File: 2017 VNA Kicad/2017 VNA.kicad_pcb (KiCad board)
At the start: 2 copper layers, 50 x 30 mm, 48 parts, among them P1 Output, P2 Input, U1 SI5351A, U2 NL7WB66, Y1 CX3225

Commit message: Our board changes
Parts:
- removed G***: LOGO, SMA:LOGO
- removed Osc1: Jumper, Resistors_SMD:R_0805
- removed R12, R13, R14, R15: 5.1k, Resistors_SMD:R_0805
- removed R16: 160, Resistors_SMD:R_0805
- removed R17: 16k, Resistors_SMD:R_0805
- removed Ref1, Test1: Jumper, Pin_Headers:Pin_Header_Straight_2x01_Pitch2.54mm
- added JP_Osc1: Osc, Pin_Headers:Pin_Header_Straight_1x02_Pitch2.54mm, F.Cu at (95.4, 93.5)
- added JP_Ref1: Ref, Pin_Headers:Pin_Header_Straight_1x02_Pitch2.54mm, F.Cu at (78.7, 88.9)
- added JP_Test1: Test, Pin_Headers:Pin_Header_Straight_1x02_Pitch2.54mm, F.Cu at (98.4, 89.6)
- added L2: 1mH, Inductors_SMD:L_1210, F.Cu at (109.5, 80.2)
- added L3: 1mH, Inductors_SMD:L_1210, F.Cu at (87.1, 76.7)
- added R3: 56, Resistors_SMD:R_0805, F.Cu at (89.3, 94.8)
- added R5: INF, Resistors_SMD:R_0805, F.Cu at (84.2, 76.0)
- added R6: 50k, Resistors_SMD:R_0805, F.Cu at (101.4, 73.4)
- C10: value 1nF -> .68uF; moved to F.Cu
- C11: value 10uF -> 0pF; moved to F.Cu
- C12: value 0.1uF -> .68uF
- C13, C6, C7, C9, L1: moved to F.Cu
- C15: value 1nF -> 27pF; moved to F.Cu
- C16: value 1nF -> 27pF
- C3: moved to B.Cu
- C8: value 1nF -> 1uF
- R10: value 16k -> 330; moved to F.Cu
- R11: value 10k -> 220; moved to F.Cu
- R4: value 51 -> INF; moved to F.Cu
- R7: value 5.1k -> 50k
- R8: value 5.1k -> 1000k; moved to F.Cu
- R9: value 5.1k -> 1000k
- moved C10 29.5 mm to (106.7, 78.1), turned to 90 degrees
- moved C3 26.0 mm to (77.4, 74.7)
- moved C6 24.0 mm to (106.7, 82.3)
- moved R8 22.3 mm to (97.4, 72.2), turned to 270 degrees
- moved R4 21.5 mm to (103.8, 72.2), turned to 90 degrees
- moved R10 20.5 mm to (91.1, 72.3), turned to 90 degrees
- moved C13 20.3 mm to (99.4, 72.2), turned to 90 degrees
- moved C15 18.0 mm to (95.0, 72.3), turned to 270 degrees
- moved C11 17.7 mm to (93.1, 72.3), turned to 270 degrees
- moved A_GND1 16.3 mm to (91.6, 75.2)
- moved R11 13.0 mm to (91.3, 79.8), turned to 270 degrees
- moved C7 12.0 mm to (98.3, 93.4), turned to 270 degrees
- moved R1 11.4 mm to (88.4, 85.4), turned to 0 degrees
- moved L1 10.1 mm to (87.3, 81.9), turned to 270 degrees
- moved R2 10.1 mm to (84.6, 84.9), turned to 270 degrees
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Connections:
- R4 pad 1: Net-(C6-Pad1) -> Net-(C10-Pad1)
- R4 pad 2: Net-(R4-Pad2) -> GND
- R7 pad 1: Net-(C8-Pad1) -> Net-(C14-Pad1)
- R7 pad 2: Net-(R7-Pad2) -> Net-(C12-Pad1)
- R8 pad 1: Net-(C10-Pad1) -> /A13
- R8 pad 2: Net-(C6-Pad1) -> Net-(C13-Pad1)
- R9 pad 1: Net-(C12-Pad1) -> /A14
- R9 pad 2: Net-(C8-Pad1) -> Net-(C14-Pad1)
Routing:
- net GND: track 246.1 -> 284.2 mm, vias 122 -> 95
- net /A13: track 9.62 -> 36.1 mm
- net Net-(C8-Pad1): track 5.72 -> 24.8 mm, vias 0 -> 1
- net Net-(C9-Pad1): track 7.33 -> 23.6 mm
- net Net-(C4-Pad2): track 5.33 -> 20.3 mm, vias 0 -> 2
- net /Ref_In: track 2.00 -> 13.4 mm, vias 0 -> 1
- net Net-(A_GND1-Pad1): track 8.57 -> 19.2 mm
- net Net-(C6-Pad1): track 5.95 -> 16.5 mm, vias 0 -> 1
- net Net-(C1-Pad2): track 17.6 -> 26.1 mm, vias 0 -> 1
- net Net-(C10-Pad1): track 5.78 -> 13.2 mm
- net /Test_In: track 14.3 -> 21.6 mm
- net /A14: track 9.69 -> 16.7 mm
- net /SDA: track 39.2 -> 44.4 mm
- net Net-(C7-Pad1): track 7.68 -> 12.1 mm
- net Net-(R7-Pad2): track 2.92 -> 0.00 mm
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
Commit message: Trying this again
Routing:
- net GND: track 284.2 -> 298.1 mm, vias 95 -> 94
- net +3V3: track 74.5 -> 76.5 mm

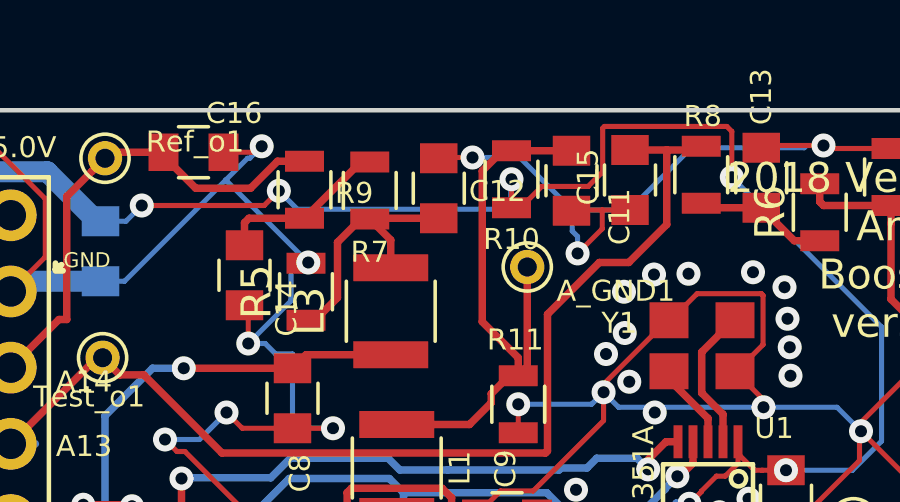
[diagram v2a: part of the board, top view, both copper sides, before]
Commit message: Fix all DRC errors
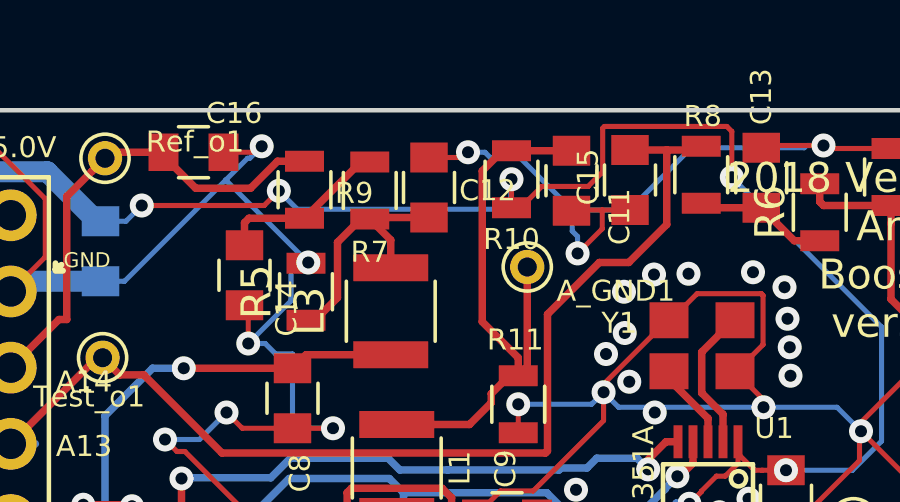
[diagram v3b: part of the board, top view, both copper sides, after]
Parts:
- moved C12 0.33 mm to (88.3, 72.6)
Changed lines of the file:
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@@
     (thickness 1.6)
     (drawings 28)
-    (tracks 654)
+    (tracks 658)
     (zones 0)
     (modules 46)
@@
   )
   (module Capacitors_SMD:C_0805 (layer F.Cu)
-    (at 88.675 72.6 90)
+    (at 88.35 72.575 90)
     (descr "Capacitor SMD 0805, reflow soldering, AVX (see smccp.pdf)")
     (tags "capacitor 0805")
@@
   (segment (start 93.302638 74.206364) (end 93.125 74.028726) (width 0.17) (layer B.Cu) (net 1))
   (segment (start 93.302638 74.772049) (end 93.302638 74.206364) (width 0.17) (layer B.Cu) (net 1))
-  (segment (start 89.8 71.575) (end 91.375 71.575) (width 0.17) (layer B.Cu) (net 1))
-  (via (at 89.8 71.575) (size 0.8) (drill 0.4) (layers F.Cu B.Cu) (net 1))
   (segment (start 88.7 71.575) (end 88.675 71.6) (width 0.17) (layer F.Cu) (net 1))
-  (segment (start 89.8 71.575) (end 88.7 71.575) (width 0.17) (layer F.Cu) (net 1))
   (via (at 82.773497 71.201198) (size 0.8) (drill 0.4) (layers F.Cu B.Cu) (net 1))
   (segment (start 81.5 71.4) (end 82.574695 71.4) (width 0.17) (layer F.Cu) (net 1))
@@
   (segment (start 82.890685 77.775) (end 83.240685 78.125) (width 0.17) (layer B.Cu) (net 1))
   (segment (start 82.325 77.775) (end 82.890685 77.775) (width 0.17) (layer B.Cu) (net 1))
+  (via (at 89.65 71.4) (size 0.8) (drill 0.4) (layers F.Cu B.Cu) (net 1))
+  (segment (start 88.35 71.575) (end 89.475 71.575) (width 0.17) (layer F.Cu) (net 1))
+  (segment (start 89.475 71.575) (end 89.65 71.4) (width 0.17) (layer F.Cu) (net 1))
+  (segment (start 90.390685 71.575) (end 91.375 71.575) (width 0.17) (layer B.Cu) (net 1))
+  (segment (start 90.215685 71.4) (end 90.390685 71.575) (width 0.17) (layer B.Cu) (net 1))
+  (segment (start 89.65 71.4) (end 90.215685 71.4) (width 0.17) (layer B.Cu) (net 1))
   (segment (start 73.319999 72.050001) (end 71.87 73.5) (width 0.7) (layer B.Cu) (net 2))
   (segment (start 75.625001 72.050001) (end 73.319999 72.050001) (width 0.7) (layer B.Cu) (net 2))
@@
   (segment (start 103.75 73.175) (end 101.5 73.175) (width 0.25) (layer F.Cu) (net 54))
   (segment (start 86.4 73.6) (end 86.375 73.625) (width 0.25) (layer F.Cu) (net 55))
-  (segment (start 88.675 73.6) (end 86.4 73.6) (width 0.25) (layer F.Cu) (net 55))
   (segment (start 84.55 77) (end 85.3 76.25) (width 0.25) (layer F.Cu) (net 55))
   (segment (start 84.25 77) (end 84.55 77) (width 0.25) (layer F.Cu) (net 55))
@@
   (segment (start 91.625 78.55) (end 91.325 78.85) (width 0.25) (layer F.Cu) (net 18))
   (segment (start 91.625 75.225) (end 91.625 78.55) (width 0.25) (layer F.Cu) (net 18))
+  (segment (start 86.425 73.575) (end 86.375 73.625) (width 0.25) (layer F.Cu) (net 55))
+  (segment (start 88.35 73.575) (end 86.425 73.575) (width 0.25) (layer F.Cu) (net 55))
   (zone (net 1) (net_name GND) (layer B.Cu) (hatch edge 0.508)
     (connect_pads (clearance 0.508))
     (min_thickness 0.254)
-    (fill (arc_segments 16) (thermal_gap 0.508) (thermal_bridge_width 0.508))
+    (fill yes (arc_segments 16) (thermal_gap 0.508) (thermal_bridge_width 0.508))
     (polygon
       (pts
@@
     (connect_pads (clearance 0.508))
     (min_thickness 0.254)
-    (fill (arc_segments 16) (thermal_gap 0.508) (thermal_bridge_width 0.508))
+    (fill yes (arc_segments 16) (thermal_gap 0.508) (thermal_bridge_width 0.508))
     (polygon
       (pts
@@
     (connect_pads (clearance 0.508))
     (min_thickness 0.254)
-    (fill (arc_segments 16) (thermal_gap 0.508) (thermal_bridge_width 0.508))
+    (fill yes (arc_segments 16) (thermal_gap 0.508) (thermal_bridge_width 0.508))
     (polygon
       (pts
@@
     (connect_pads (clearance 0.508))
     (min_thickness 0.254)
-    (fill (arc_segments 16) (thermal_gap 0.508) (thermal_bridge_width 0.508))
+    (fill yes (arc_segments 16) (thermal_gap 0.508) (thermal_bridge_width 0.508))
     (polygon
       (pts
@@
     (connect_pads (clearance 0.508))
     (min_thickness 0.254)
-    (fill (arc_segments 16) (thermal_gap 0.508) (thermal_bridge_width 0.508))
+    (fill yes (arc_segments 16) (thermal_gap 0.508) (thermal_bridge_width 0.508))
     (polygon
       (pts

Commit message: Hopefully ready for printing now
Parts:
- removed C11: 0pF, Capacitors_SMD:C_0805
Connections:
- R4 pad 1: Net-(C10-Pad1) -> Net-(C13-Pad1)
- R5 pad 1: Net-(C12-Pad1) -> Net-(C14-Pad1)
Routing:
- net Net-(C13-Pad1): track 4.47 -> 12.5 mm, vias 0 -> 2
- net Net-(C12-Pad1): track 8.55 -> 4.25 mm
- net Net-(C14-Pad1): track 5.76 -> 9.66 mm
- net Net-(A_GND1-Pad1): track 19.2 -> 17.2 mm
- net Net-(C10-Pad1): track 13.2 -> 12.1 mm
- net GND: vias 94 -> 117
- net (no net): vias 0 -> 3
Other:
- board text added: "2018 Vector Network Analyzer BoosterPack version 0.6"
- board text added: "Jacob Priddy WWU 5/28/2018"
- board text removed: "2018 Vector Network Analyzer BoosterPack version 0.4"
- board text removed: "Rob Frohne WWU 1/14/2018"

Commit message: A little clean up of the title blocks, etc.
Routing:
- net /Test_In: track 21.6 -> 18.1 mm, vias 1 -> 0
- net (no net): vias 3 -> 1
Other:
- board text added: "WWU-VNA v 0.6"
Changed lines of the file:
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@@
-(kicad_pcb (version 20171130) (host pcbnew "(5.0.0-rc2-35-gda6600525)")
+(kicad_pcb (version 20171130) (host pcbnew 5.0.0-rc2-unknown-6090f90~65~ubuntu18.04.1)
   (general
     (thickness 1.6)
-    (drawings 28)
-    (tracks 702)
+    (drawings 29)
+    (tracks 693)
     (zones 0)
     (modules 45)
@@
     (34 B.Paste user)
     (35 F.Paste user)
-    (36 B.SilkS user hide)
-    (37 F.SilkS user hide)
+    (36 B.SilkS user)
+    (37 F.SilkS user)
     (38 B.Mask user)
     (39 F.Mask user)
@@
       (hpglpennumber 1)
       (hpglpenspeed 20)
-      (hpglpendiameter 15.000000)
+      (hpglpendiameter 15)
       (psnegative false)
       (psa4output false)
@@
     (descr "module 1 pin (ou trou mecanique de percage)")
     (tags DEV)
-    (fp_text reference LO_Q1 (at 2.6 -0.05) (layer F.SilkS)
+    (fp_text reference LO_Q1 (at 2.4 1.13) (layer F.SilkS)
       (effects (font (size 0.7 0.7) (thickness 0.15)))
     )
@@
     (descr "module 1 pin (ou trou mecanique de percage)")
     (tags DEV)
-    (fp_text reference Ref_o1 (at -2.1 -1.125) (layer F.SilkS)
+    (fp_text reference Ref_o1 (at -2.32 -1.02) (layer F.SilkS)
       (effects (font (size 0.7 0.7) (thickness 0.15)))
     )
@@
     (descr "Through hole straight pin header, 1x02, 2.54mm pitch, single row")
     (tags "Through hole pin header THT 1x02 2.54mm single row")
-    (fp_text reference JP_Osc1 (at 1.8 1.24 180) (layer F.SilkS)
-      (effects (font (size 1 1) (thickness 0.15)))
+    (fp_text reference JP_Osc1 (at 1.945 1.105 180) (layer F.SilkS)
+      (effects (font (size 0.762 0.762) (thickness 0.15)))
     )
     (fp_text value Osc (at 0 4.87 270) (layer F.Fab)
@@
     (descr "Through hole straight pin header, 1x02, 2.54mm pitch, single row")
     (tags "Through hole pin header THT 1x02 2.54mm single row")
-    (fp_text reference JP_Ref1 (at 0 -2.33) (layer F.SilkS)
+    (fp_text reference JP_Ref1 (at 1.19 -2.31) (layer F.SilkS)
       (effects (font (size 1 1) (thickness 0.15)))
     )
@@
     (descr "Through hole straight pin header, 1x02, 2.54mm pitch, single row")
     (tags "Through hole pin header THT 1x02 2.54mm single row")
-    (fp_text reference JP_Test1 (at 0.3 5.4 90) (layer F.SilkS)
+    (fp_text reference JP_Test1 (at -1.32 7.05 180) (layer F.SilkS)
       (effects (font (size 1 1) (thickness 0.15)))
     )
@@
     )
   )
+  (gr_text "WWU-VNA\nv 0.6" (at 106.32 87.75) (layer F.SilkS)
+    (effects (font (size 1.016 1.016) (thickness 0.254)))
+  )
   (gr_line (start 75.9 75.35) (end 76.15 75.35) (layer F.SilkS) (width 0.2))
   (gr_line (start 75.9 75.3) (end 75.9 75.1) (layer F.SilkS) (width 0.2))
@@
     (effects (font (size 0.7 0.7) (thickness 0.15)))
   )
-  (gr_text 5.0V (at 74.7 71.35) (layer F.SilkS)
+  (gr_text 5.0V (at 74.98 71.69) (layer F.SilkS)
     (effects (font (size 0.7 0.7) (thickness 0.15)))
   )
@@
     (arrow2b (pts (xy 70 60) (xy 71.126504 59.413579)))
   )
-  (via (at 83.05 89.175) (size 0.8) (drill 0.4) (layers F.Cu B.Cu) (net 0))
-  (via (at 82.125 86.65) (size 0.8) (drill 0.4) (layers F.Cu B.Cu) (net 0))
   (via (at 94.575 82.675) (size 0.8) (drill 0.4) (layers F.Cu B.Cu) (net 0))
   (via (at 84.325 75.075) (size 0.8) (drill 0.4) (layers F.Cu B.Cu) (net 1))
@@
   (segment (start 83.775 91.9) (end 84.15 91.9) (width 1) (layer F.Cu) (net 3))
   (segment (start 91.221716 88.538283) (end 91.249999 88.51) (width 1) (layer F.Cu) (net 3))
-  (segment (start 83.775 91.9) (end 84.29435 91.9) (width 0.17) (layer F.Cu) (net 3))
-  (segment (start 85.597175 91.16286) (end 85.597175 90.597175) (width 0.17) (layer B.Cu) (net 3))
-  (segment (start 85.197176 90.997174) (end 85.597175 90.597175) (width 0.17) (layer F.Cu) (net 3))
-  (segment (start 84.29435 91.9) (end 85.197176 90.997174) (width 0.17) (layer F.Cu) (net 3))
-  (segment (start 85.597175 91.397175) (end 85.597175 91.16286) (width 0.17) (layer B.Cu) (net 3))
-  (segment (start 85.8 91.6) (end 85.597175 91.397175) (width 0.17) (layer B.Cu) (net 3))
-  (via (at 85.597175 90.597175) (size 0.8) (drill 0.4) (layers F.Cu B.Cu) (net 3))
   (segment (start 82.15 91.9) (end 83.775 91.9) (width 1) (layer F.Cu) (net 3) (status 10))
   (segment (start 91.249999 88.51) (end 91.6 88.51) (width 0.17) (layer F.Cu) (net 3) (status 20))
@@
   (segment (start 101.375 72.45) (end 101.675 72.45) (width 0.25) (layer F.Cu) (net 54))
   (segment (start 86.4 73.6) (end 86.375 73.625) (width 0.25) (layer F.Cu) (net 55))
-  (segment (start 84.25 77) (end 84.55 77) (width 0.25) (layer F.Cu) (net 57))
   (segment (start 86.075 73.625) (end 86.375 73.625) (width 0.25) (layer F.Cu) (net 55))
   (segment (start 87.075 74.325) (end 86.375 73.625) (width 0.25) (layer F.Cu) (net 55))
@@
   (segment (start 102.725 74.859315) (end 102.6 74.734315) (width 0.25) (layer F.Cu) (net 56))
   (segment (start 102.725 75.425) (end 102.725 74.859315) (width 0.25) (layer F.Cu) (net 56))
+  (segment (start 84.25 77) (end 84.55 77) (width 0.25) (layer F.Cu) (net 57))
   (segment (start 86.075 71.725) (end 84.2 73.6) (width 0.25) (layer F.Cu) (net 57))
   (segment (start 86.375 71.725) (end 86.075 71.725) (width 0.25) (layer F.Cu) (net 57))
